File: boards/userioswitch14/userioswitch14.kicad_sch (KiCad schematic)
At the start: 16 parts, among them IC1 SN3257QPWRQ1, IC2 SN3257QPWRQ1, J1 692112030100, J2 Conn_02x03_Odd_Even, J3 692122030100, J4 692122030100, J5 692122030100, J6 692122030100, J7 Conn_02x05_Odd_Even

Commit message: New
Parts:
- removed J3, J5: 692122030100, 692122030100, symbol mouser:692122030100
- C1, C2: value C_Polarized -> 10u; symbol Device:C_Polarized -> Device:C
- IC1, IC2: footprint SOP65P640X120-16N -> mouser:SOP65P640X120-16N
- J4, J6: footprint 692122030100 -> mouser:692122030100
- J7: value Conn_02x05_Odd_Even -> Header; footprint Connector_PinHeader_2.54mm:PinHeader_2x05_P2.54mm_Vertical -> Connector_PinHeader_2.54mm:PinHeader_2x07_P2.54mm_Vertical; symbol Connector_Generic:Conn_02x05_Odd_Even -> Connector_Generic:Conn_02x07_Odd_Even
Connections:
- net D2: now also IC1.9 (D3); no longer IC2.7 (D2)
- net D3: now also IC1.7 (D2); no longer IC2.9 (D3)
- net D4: now also IC1.4 (D1); no longer IC2.12 (D4)
- net D5: now also IC2.7 (D2); no longer IC1.4 (D1)
- net D6: now also IC2.12 (D4); no longer IC1.7 (D2)
- net D7: now also IC2.9 (D3); no longer IC1.9 (D3)
- net GND: now also J7.12 (Pin_12), J7.2 (Pin_2), J7.4 (Pin_4), J7.6 (Pin_6)
- net S1A: now also J7.9 (Pin_9); no longer J7.4 (Pin_4)
- net S2A: now also IC1.11 (S3A), J7.5 (Pin_5); no longer IC2.5 (S2A), J7.6 (Pin_6)
- net S2B: now also IC1.10 (S3B); no longer IC2.6 (S2B)
- net S3A: now also IC1.5 (S2A), J7.1 (Pin_1); no longer IC2.11 (S3A), J7.9 (Pin_9)
- net S3B: now also IC1.6 (S2B); no longer IC2.10 (S3B)
- net S4A: now also IC1.2 (S1A), J7.3 (Pin_3); no longer IC2.14 (S4A), J7.7 (Pin_7)
- net S4B: now also IC1.3 (S1B); no longer IC2.13 (S4B)
- net S5A: now also IC2.5 (S2A), J7.7 (Pin_7); no longer IC1.2 (S1A), J7.5 (Pin_5)
- net S5B: now also IC2.6 (S2B); no longer IC1.3 (S1B)
- net S6A: now also IC2.14 (S4A), J7.11 (Pin_11); no longer IC1.5 (S2A), J7.3 (Pin_3)
- net S6B: now also IC2.13 (S4B); no longer IC1.6 (S2B)
- net S7A: now also IC2.11 (S3A), J7.13 (Pin_13); no longer IC1.11 (S3A), J7.1 (Pin_1)
- net S7B: now also IC2.10 (S3B); no longer IC1.10 (S3B)
- net VBUSA: now also J7.14 (Pin_14); no longer J7.2 (Pin_2)

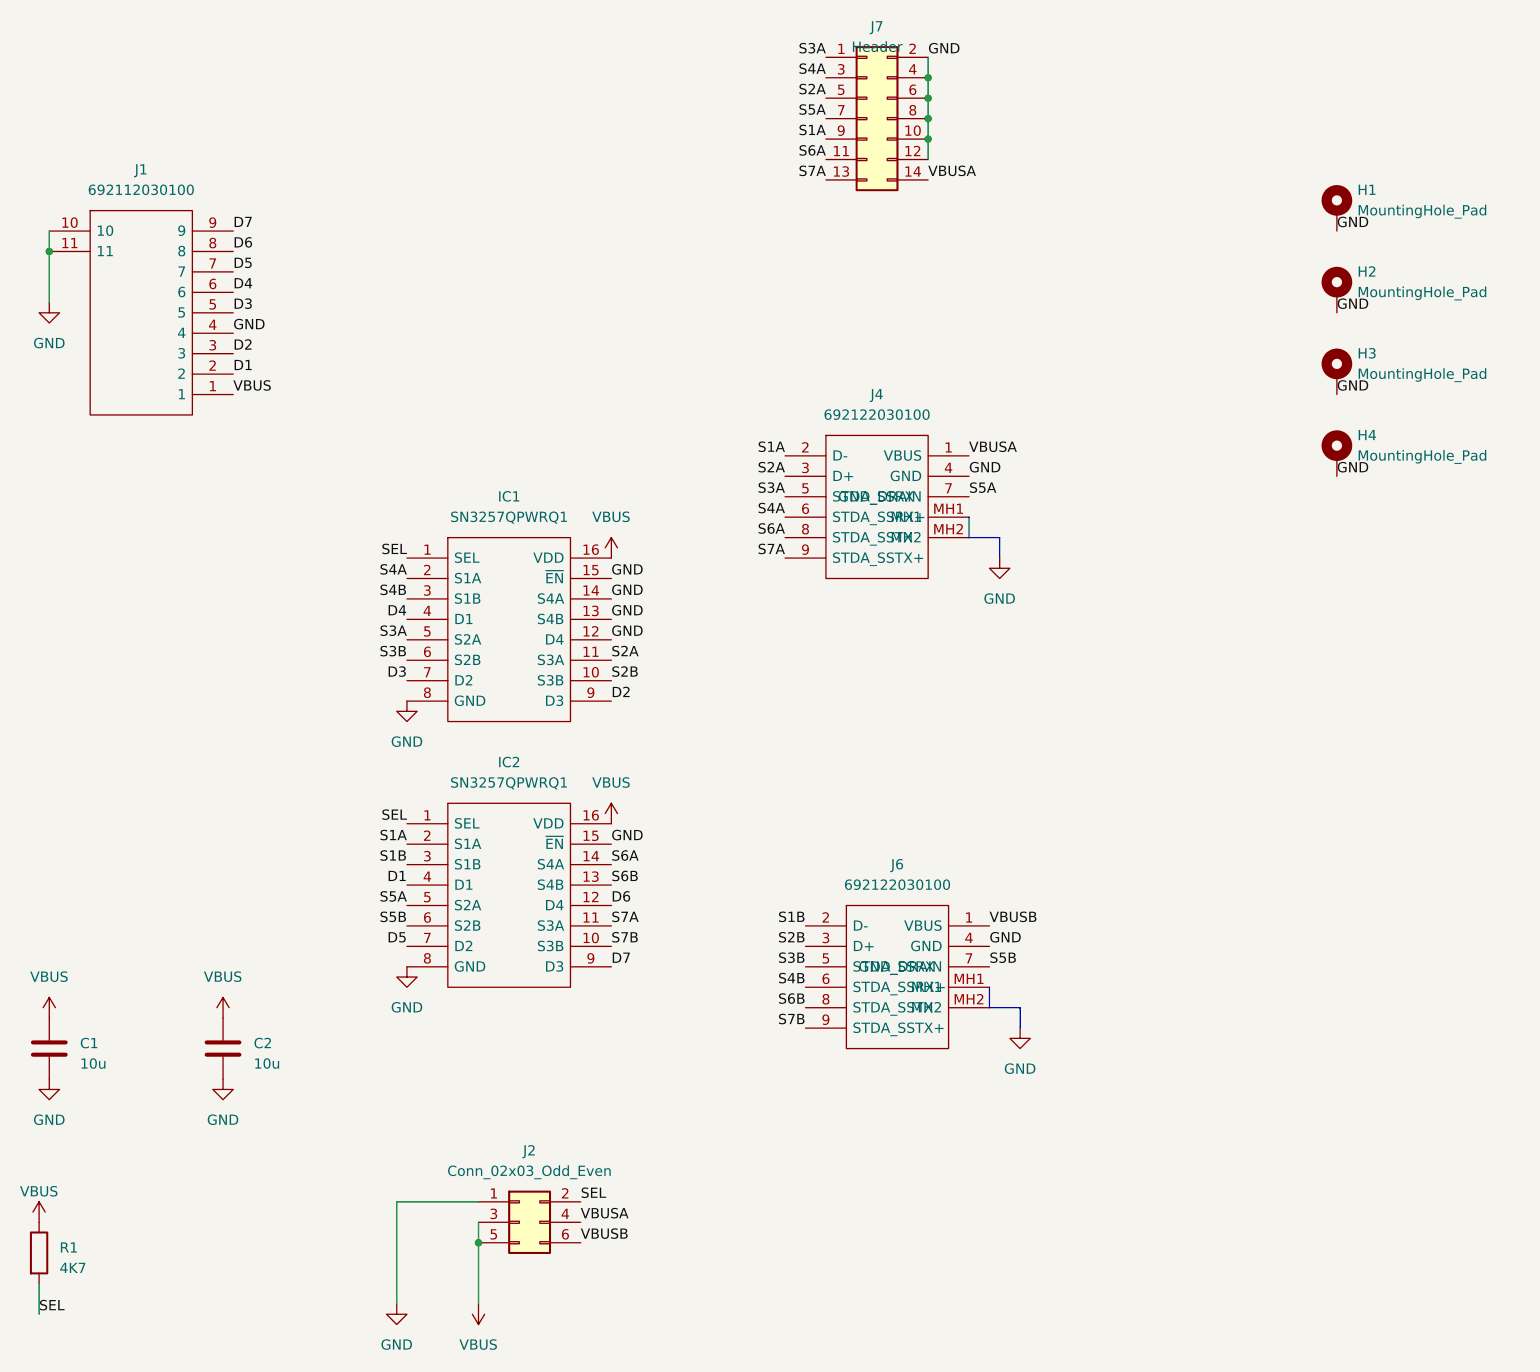
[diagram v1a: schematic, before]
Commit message: Move to 14 pin headers for switch with off-board adapters
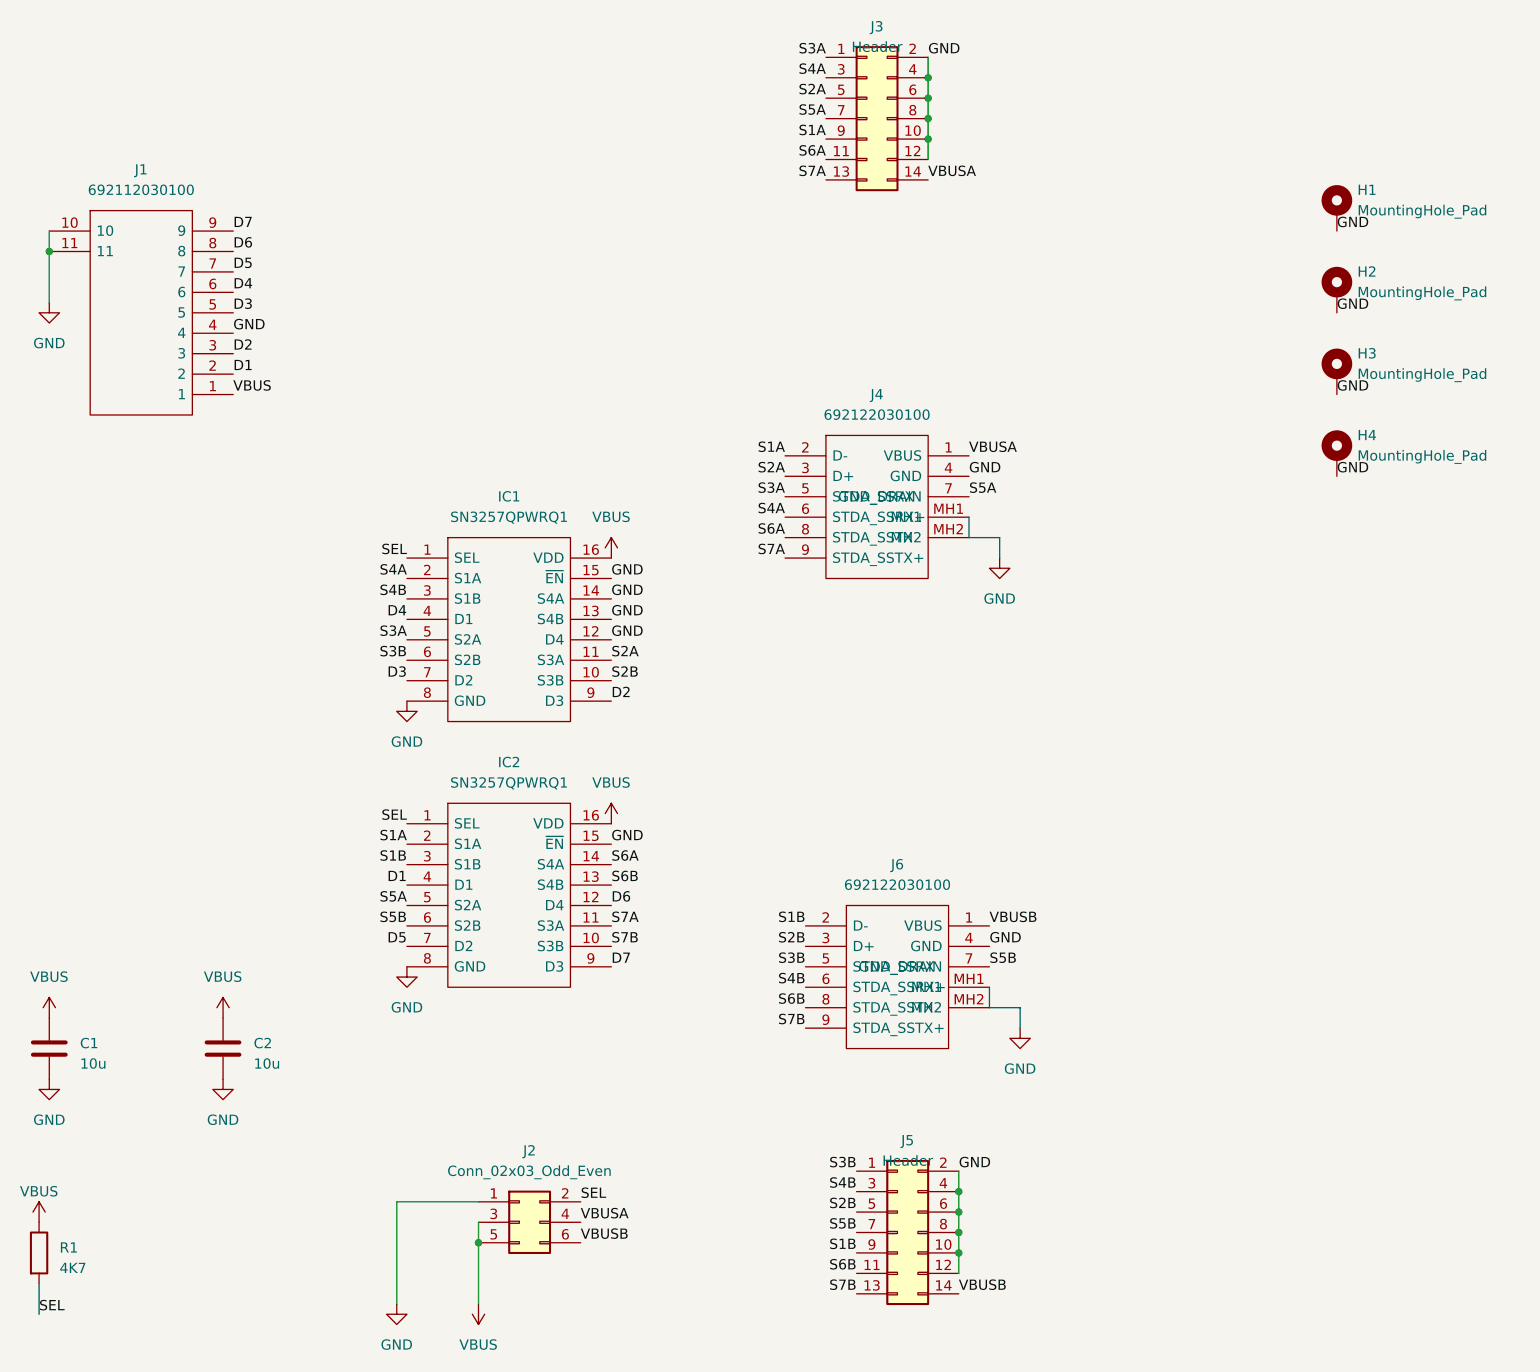
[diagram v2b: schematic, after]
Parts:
- added J5: Header, Connector_PinHeader_2.54mm:PinHeader_2x07_P2.54mm_Vertical, symbol Connector_Generic:Conn_02x07_Odd_Even
- renumbered J7 to J3
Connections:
- net GND: now also J5.10 (Pin_10), J5.12 (Pin_12), J5.2 (Pin_2), J5.4 (Pin_4), J5.6 (Pin_6), J5.8 (Pin_8)
- net S1B: now also J5.9 (Pin_9)
- net S2B: now also J5.5 (Pin_5)
- net S3B: now also J5.1 (Pin_1)
- net S4B: now also J5.3 (Pin_3)
- net S5B: now also J5.7 (Pin_7)
- net S6B: now also J5.11 (Pin_11)
- net S7B: now also J5.13 (Pin_13)
- net VBUSB: now also J5.14 (Pin_14)
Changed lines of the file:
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@@
 (kicad_sch (version 20230121) (generator eeschema)
   (paper "A4")
+  (junction (at 149.86 166.37) (diameter 0) (color 0 0 0 0)
+  )
+  (junction (at 149.86 161.29) (diameter 0) (color 0 0 0 0)
+  )
   (junction (at 90.17 165.1) (diameter 0) (color 0 0 0 0)
   )
   (junction (at 36.83 41.91) (diameter 0) (color 0 0 0 0)
   )
+  (junction (at 149.86 158.75) (diameter 0) (color 0 0 0 0)
+  )
   (junction (at 146.05 27.94) (diameter 0) (color 0 0 0 0)
   )
@@
   (junction (at 146.05 25.4) (diameter 0) (color 0 0 0 0)
   )
+  (junction (at 149.86 163.83) (diameter 0) (color 0 0 0 0)
+  )
   (junction (at 146.05 22.86) (diameter 0) (color 0 0 0 0)
   )
@@
     (stroke (width 0) (type default))
   )
+  (wire (pts (xy 149.86 156.21) (xy 149.86 158.75))
+    (stroke (width 0) (type default))
+  )
   (wire (pts (xy 146.05 22.86) (xy 146.05 25.4))
     (stroke (width 0) (type default))
@@
     (stroke (width 0) (type default))
   )
+  (wire (pts (xy 149.86 161.29) (xy 149.86 163.83))
+    (stroke (width 0) (type default))
+  )
   (bus (pts (xy 153.67 133.35) (xy 153.67 135.89))
     (stroke (width 0) (type default))
@@
     (stroke (width 0) (type default))
   )
+  (wire (pts (xy 149.86 163.83) (xy 149.86 166.37))
+    (stroke (width 0) (type default))
+  )
   (wire (pts (xy 146.05 20.32) (xy 146.05 22.86))
     (stroke (width 0) (type default))
@@
     (stroke (width 0) (type default))
   )
+  (wire (pts (xy 149.86 158.75) (xy 149.86 161.29))
+    (stroke (width 0) (type default))
+  )
   (bus (pts (xy 151.13 77.47) (xy 154.94 77.47))
     (stroke (width 0) (type default))
@@
     (stroke (width 0) (type default))
   )
+  (wire (pts (xy 149.86 166.37) (xy 149.86 168.91))
+    (stroke (width 0) (type default))
+  )
   (wire (pts (xy 146.05 25.4) (xy 146.05 27.94))
     (stroke (width 0) (type default))
@@
     (effects (font (size 1.27 1.27)) (justify right bottom))
   )
+  (label "VBUSB" (at 149.86 171.45 0) (fields_autoplaced)
+    (effects (font (size 1.27 1.27)) (justify left bottom))
+  )
   (label "GND" (at 196.85 39.37 0) (fields_autoplaced)
     (effects (font (size 1.27 1.27)) (justify left bottom))
@@
     (effects (font (size 1.27 1.27)) (justify left bottom))
   )
+  (label "S1B" (at 137.16 166.37 180) (fields_autoplaced)
+    (effects (font (size 1.27 1.27)) (justify right bottom))
+  )
   (label "SEL" (at 81.28 80.01 180) (fields_autoplaced)
     (effects (font (size 1.27 1.27)) (justify right bottom))
@@
     (effects (font (size 1.27 1.27)) (justify left bottom))
   )
+  (label "S2B" (at 137.16 161.29 180) (fields_autoplaced)
+    (effects (font (size 1.27 1.27)) (justify right bottom))
+  )
   (label "GND" (at 153.67 128.27 0) (fields_autoplaced)
     (effects (font (size 1.27 1.27)) (justify left bottom))
@@
     (effects (font (size 1.27 1.27)) (justify left bottom))
   )
+  (label "S5B" (at 137.16 163.83 180) (fields_autoplaced)
+    (effects (font (size 1.27 1.27)) (justify right bottom))
+  )
+  (label "S6B" (at 137.16 168.91 180) (fields_autoplaced)
+    (effects (font (size 1.27 1.27)) (justify right bottom))
+  )
   (label "S6A" (at 133.35 30.48 180) (fields_autoplaced)
     (effects (font (size 1.27 1.27)) (justify right bottom))
@@
     (effects (font (size 1.27 1.27)) (justify left bottom))
   )
+  (label "S3B" (at 137.16 156.21 180) (fields_autoplaced)
+    (effects (font (size 1.27 1.27)) (justify right bottom))
+  )
   (label "SEL" (at 81.28 113.03 180) (fields_autoplaced)
     (effects (font (size 1.27 1.27)) (justify right bottom))
@@
     (effects (font (size 1.27 1.27)) (justify left bottom))
   )
+  (label "S4B" (at 137.16 158.75 180) (fields_autoplaced)
+    (effects (font (size 1.27 1.27)) (justify right bottom))
+  )
   (label "D3" (at 81.28 95.25 180) (fields_autoplaced)
     (effects (font (size 1.27 1.27)) (justify right bottom))
@@
     (effects (font (size 1.27 1.27)) (justify right bottom))
   )
+  (label "S7B" (at 137.16 171.45 180) (fields_autoplaced)
+    (effects (font (size 1.27 1.27)) (justify right bottom))
+  )
   (label "S5A" (at 133.35 25.4 180) (fields_autoplaced)
     (effects (font (size 1.27 1.27)) (justify right bottom))
@@
   )
   (label "VBUSB" (at 102.87 165.1 0) (fields_autoplaced)
+    (effects (font (size 1.27 1.27)) (justify left bottom))
+  )
+  (label "GND" (at 149.86 156.21 0) (fields_autoplaced)
     (effects (font (size 1.27 1.27)) (justify left bottom))
   )
@@
         (path "/19ab583a-eddd-45c3-bdfa-c7623083b85c"
           (reference "H3") (unit 1)
+        )
+      )
+    )
+  )
+  (symbol (lib_id "Connector_Generic:Conn_02x07_Odd_Even") (at 142.24 163.83 0) (unit 1)
+    (in_bom yes) (on_board yes) (dnp no) (fields_autoplaced)
+    (property "Reference" "J5" (at 143.51 152.4 0)
+      (effects (font (size 1.27 1.27)))
+    )
+    (property "Value" "Header" (at 143.51 154.94 0)
+      (effects (font (size 1.27 1.27)))
+    )
+    (property "Footprint" "Connector_PinHeader_2.54mm:PinHeader_2x07_P2.54mm_Vertical" (at 142.24 163.83 0)
+      (effects (font (size 1.27 1.27)) hide)
+    )
+    (property "Datasheet" "~" (at 142.24 163.83 0)
+      (effects (font (size 1.27 1.27)) hide)
+    )
+    (pin "1")
+    (pin "10")
+    (pin "11")
+    (pin "12")
+    (pin "13")
+    (pin "14")
+    (pin "2")
+    (pin "3")
+    (pin "4")
+    (pin "5")
+    (pin "6")
+    (pin "7")
+    (pin "8")
+    (pin "9")
+    (instances
+      (project "userioswitch14"
+        (path "/19ab583a-eddd-45c3-bdfa-c7623083b85c"
+          (reference "J5") (unit 1)
         )
       )
@@
   (symbol (lib_id "Connector_Generic:Conn_02x07_Odd_Even") (at 138.43 25.4 0) (unit 1)
     (in_bom yes) (on_board yes) (dnp no) (fields_autoplaced)
-    (property "Reference" "J7" (at 139.7 13.97 0)
+    (property "Reference" "J3" (at 139.7 13.97 0)
       (effects (font (size 1.27 1.27)))
     )
@@
       (project "userioswitch14"
         (path "/19ab583a-eddd-45c3-bdfa-c7623083b85c"
-          (reference "J7") (unit 1)
-        )
-      )
+          (reference "J3") (unit 1)
+        )
+      )
